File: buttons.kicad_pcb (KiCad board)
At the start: 2 copper layers, 30.7 x 34.9 mm, 16 parts, among them J1 Conn_01x02, J3 Conn_01x10, SW1 SW_SPST, SW2 SW_SPST, U1 TLC555xP, U2 74LS14

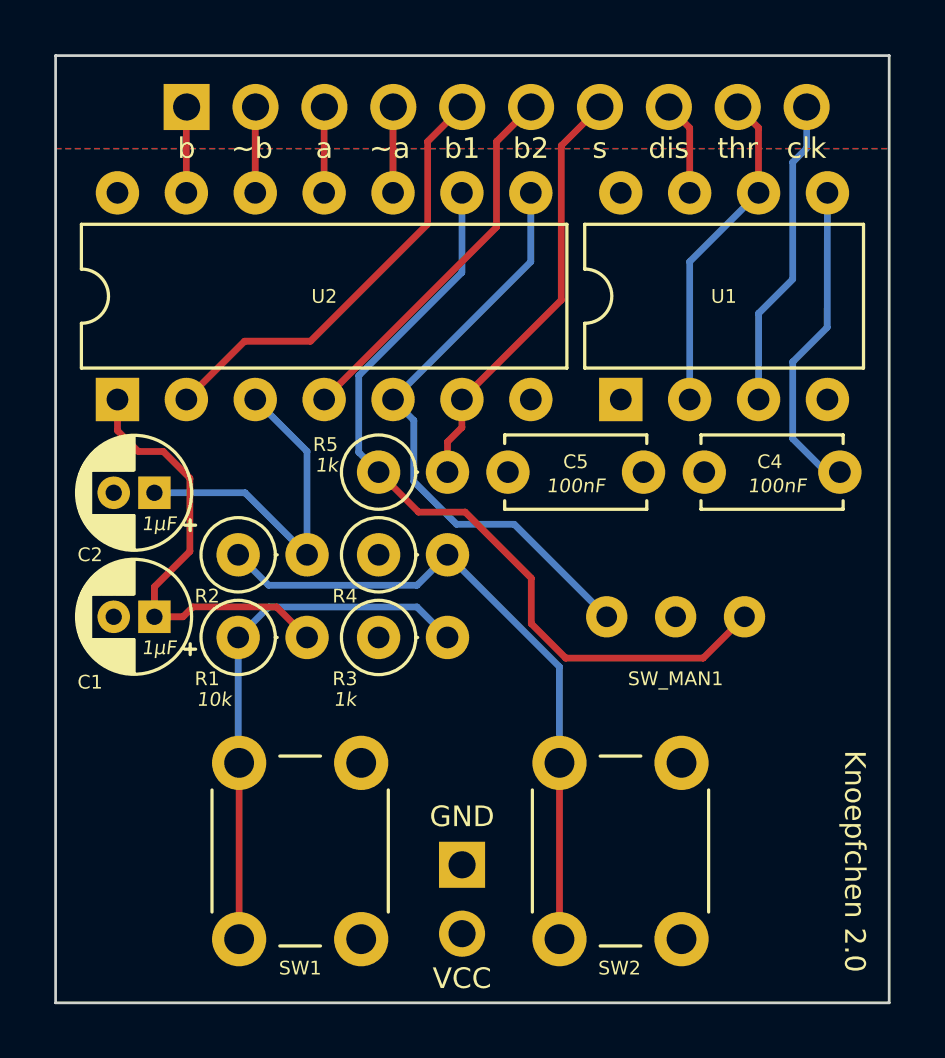
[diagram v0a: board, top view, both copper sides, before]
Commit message: simplified pcb layout
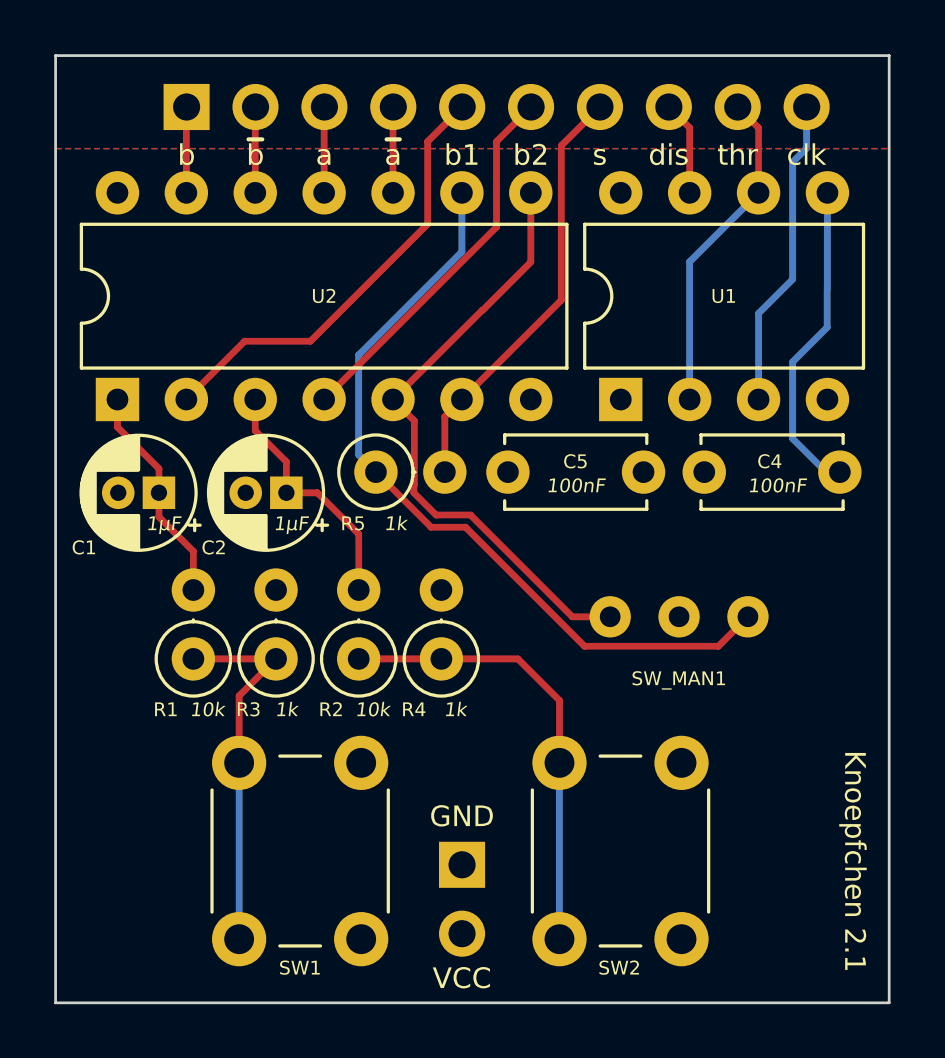
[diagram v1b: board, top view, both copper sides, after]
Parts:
- moved R2 5.87 mm to (77.5, 66.1), turned to 90 degrees
- moved C2 4.87 mm to (74.8, 59.9)
- moved C1 4.58 mm to (70.1, 59.9)
- moved R4 4.48 mm to (80.5, 66.1), turned to 90 degrees
- moved R3 3.86 mm to (74.4, 66.1), turned to 90 degrees
- moved R1 1.83 mm to (71.4, 66.1), turned to 90 degrees
- moved SW_MAN1 0.13 mm to (89.3, 64.5)
- moved R5 0.10 mm to (78.1, 59.2)
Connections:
- R3 pad 1: VCC -> Net-(R1-Pad1)
- R3 pad 2: Net-(R1-Pad1) -> VCC
- R4 pad 1: VCC -> Net-(R2-Pad1)
- R4 pad 2: Net-(R2-Pad1) -> VCC
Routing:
- net Net-(C1-Pad1): track 16.4 -> 8.18 mm
- net Net-(R2-Pad1): track 24.5 -> 16.8 mm
- net Net-(R1-Pad1): track 19.8 -> 13.9 mm
- net Net-(C2-Pad1): track 13.1 -> 9.27 mm
- net Net-(R5-Pad1): track 30.1 -> 29.0 mm
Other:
- board text added: "Knoepfchen 2.1"
- board text added: "~{a}"
- board text added: "~{b}"
- board text removed: "Knoepfchen 2.0"
- board text removed: "~a"
- board text removed: "~b"

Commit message: smaller refinements
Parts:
- moved R2 0.26 mm to (77.2, 66.0)
- moved R4 0.26 mm to (80.3, 66.0)
- moved R1 0.26 mm to (71.1, 66.0)
- moved R3 0.26 mm to (74.2, 66.0)
- moved SW_MAN1 0.25 mm to (89.0, 64.5)
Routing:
- net Net-(R5-Pad1): track 29.0 -> 28.2 mm

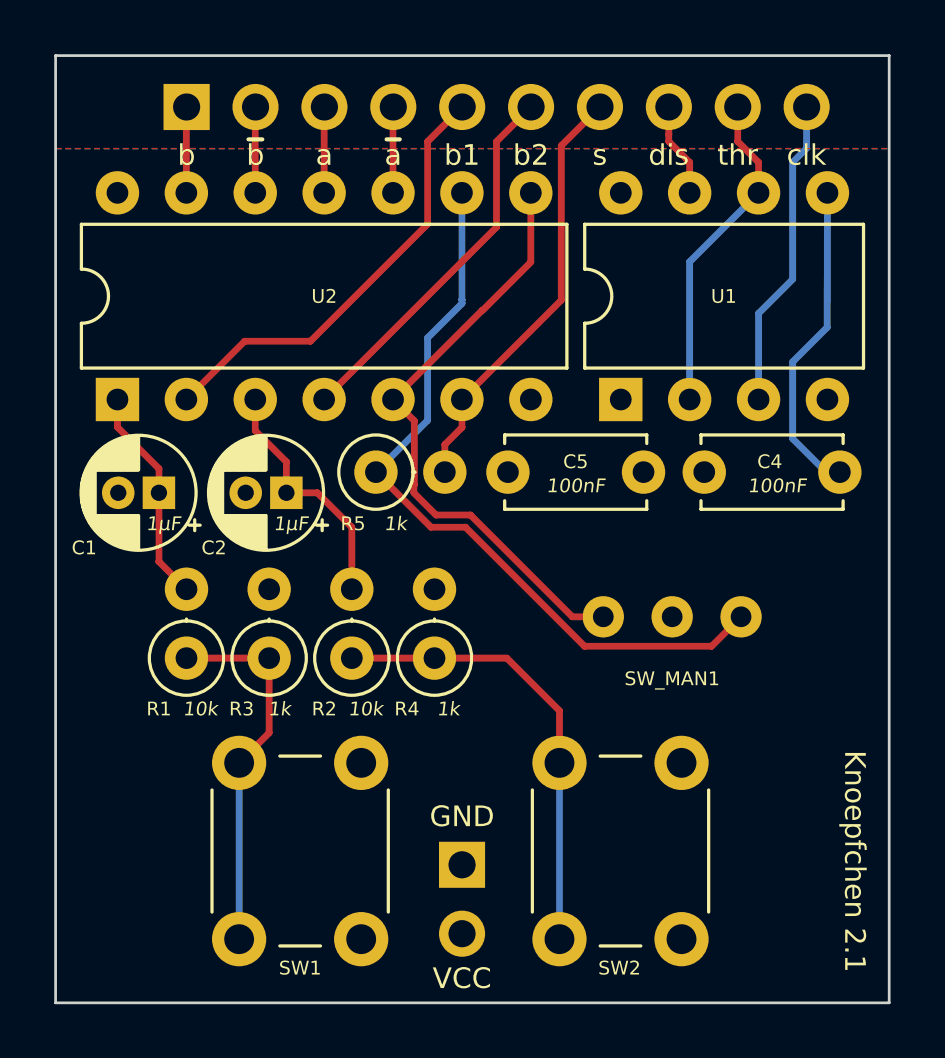
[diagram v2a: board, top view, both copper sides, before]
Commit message: changed SPDT switch to standard jumper rail.
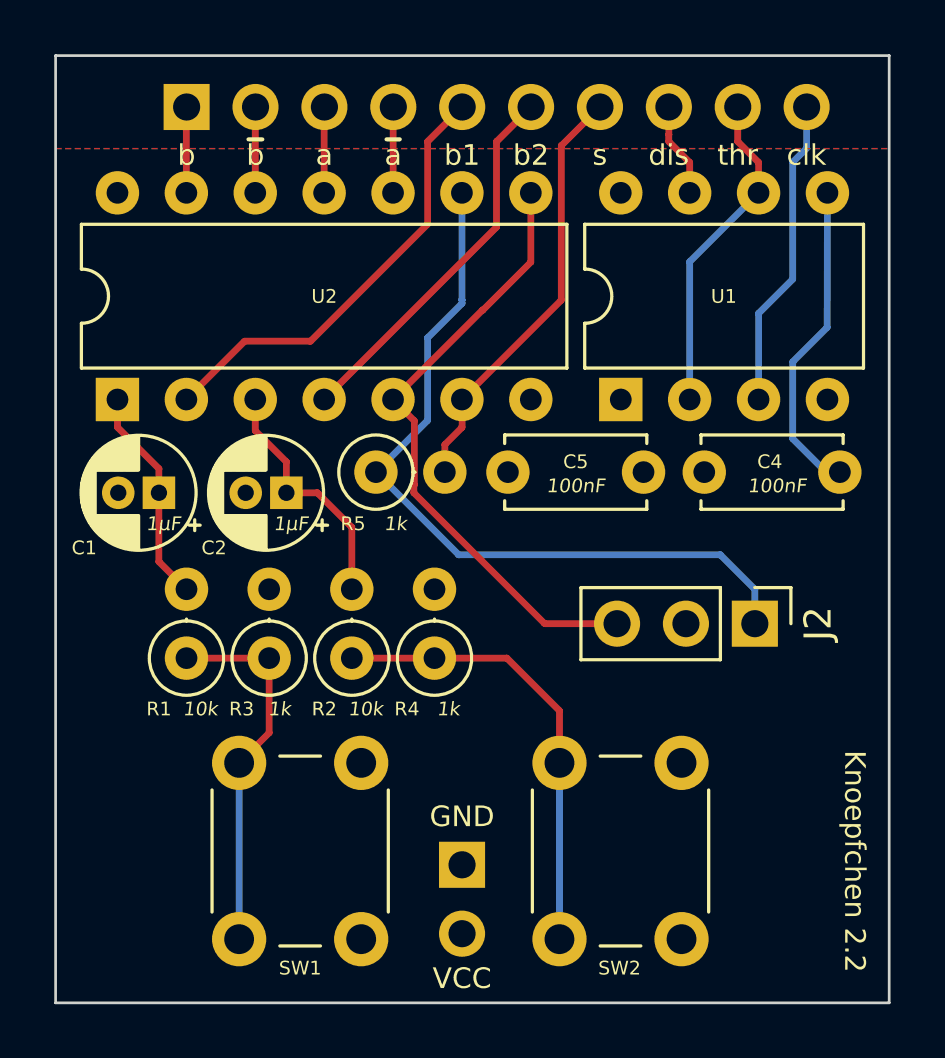
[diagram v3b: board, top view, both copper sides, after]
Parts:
- removed SW_MAN1: SW_SPDT, Button_Switch_THT:Apem 25000N series
- added J2: Conn_01x03_Pin, Connector_PinHeader_2.54mm:PinHeader_1x03_P2.54mm_Vertical, F.Cu at (92.1, 64.8)
- J1: value Conn_01x02 -> Conn_01x02_Pin
- J3: value Conn_01x10 -> Conn_01x10_Pin
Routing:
- net Net-(J2-Pin_3): track 22.4 -> 23.0 mm
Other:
- board text added: "Knoepfchen 2.2"
- board text removed: "Knoepfchen 2.1"
